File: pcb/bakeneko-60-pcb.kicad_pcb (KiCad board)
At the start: 2 copper layers, 284.7 x 94.2 mm, 147 parts, among them J1 JST SH 4-pin, J2 AVR-ISP-6, SW1 Reset, U1 SRV05-4, U2 ATmega32U4-AU, Y1 16MHz

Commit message: add fn1
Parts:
- added D64: 1N4148, Diode_SMD:D_SOD-123, F.Cu at (68.7, 86.1)
- added MX74: 1.25u, MX_Only:MXOnly-1.25U-NoLED, F.Cu at (82.8, 85.2)
- MX69: value 1.5u -> 1.25u; footprint MX_Only:MXOnly-1.5U-NoLED -> MX_Only:MXOnly-1.25U-NoLED
- MX70: value 7u -> 2.75u; footprint MX_Only:MXOnly-7U-ReversedStabilizers-NoLED -> MX_Only:MXOnly-2.75U-ReversedStabilizers-NoLED
- moved MX69 2.38 mm to (59.0, 85.2)
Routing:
- net COL4: track 143.4 -> 165.4 mm
- net Net-(D64-Pad2): track 0.00 -> 11.1 mm
- net Net-(D58-Pad2): track 9.20 -> 6.82 mm
- net COL2: track 142.7 -> 143.7 mm

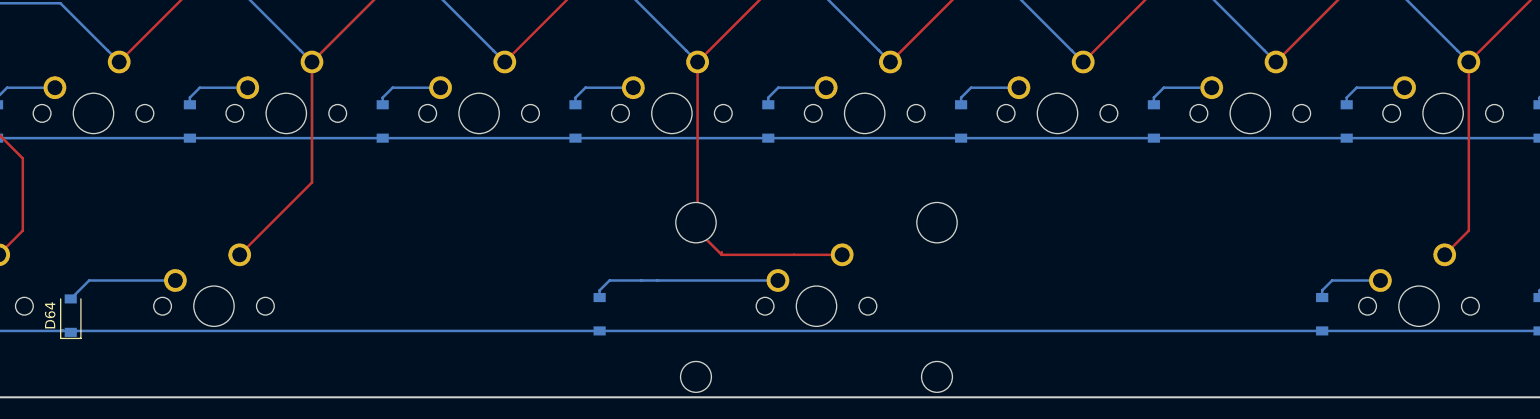
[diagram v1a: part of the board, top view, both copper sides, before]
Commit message: bottom row done except for diodes wrong side
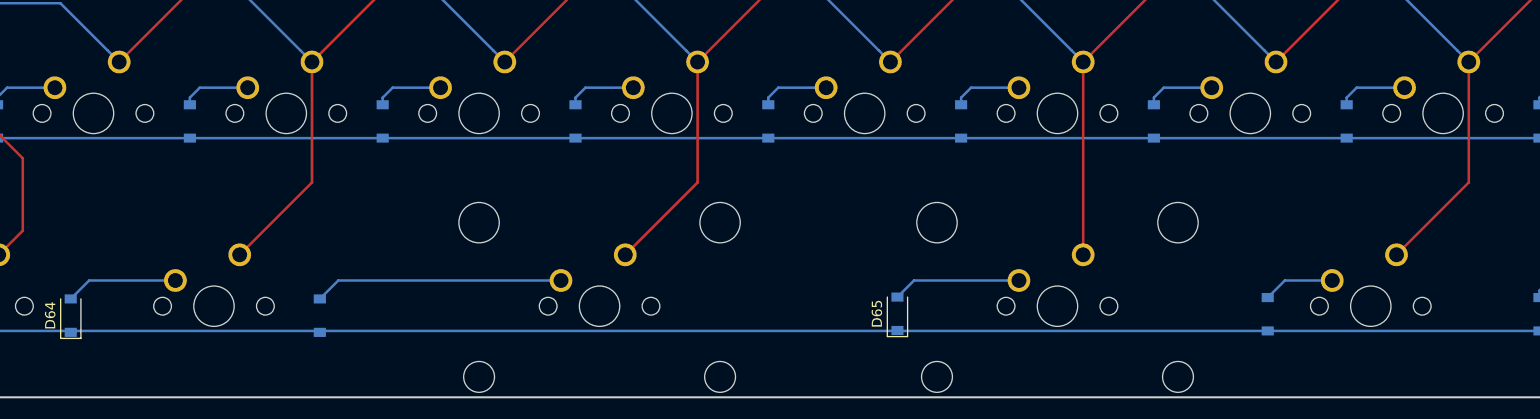
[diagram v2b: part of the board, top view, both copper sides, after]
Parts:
- added D65: 1N4148, Diode_SMD:D_SOD-123, F.Cu at (150.3, 86.0)
- added MX75: 2u, MX_Only:MXOnly-2U-ReversedStabilizers-NoLED, F.Cu at (166.2, 85.2)
- moved D59 27.6 mm to (93.3, 86.1)
- moved MX70 21.4 mm to (120.9, 85.2)
- moved D60 5.38 mm to (186.9, 86.0)
- moved MX63 4.76 mm to (197.1, 85.2)
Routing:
- net COL8: track 217.4 -> 236.4 mm
- net Net-(MX75-Pad1): track 0.00 -> 12.7 mm
- net COL6: track 212.3 -> 202.1 mm
- net Net-(D59-Pad2): track 18.7 -> 24.6 mm
- net COL10: track 274.7 -> 276.7 mm

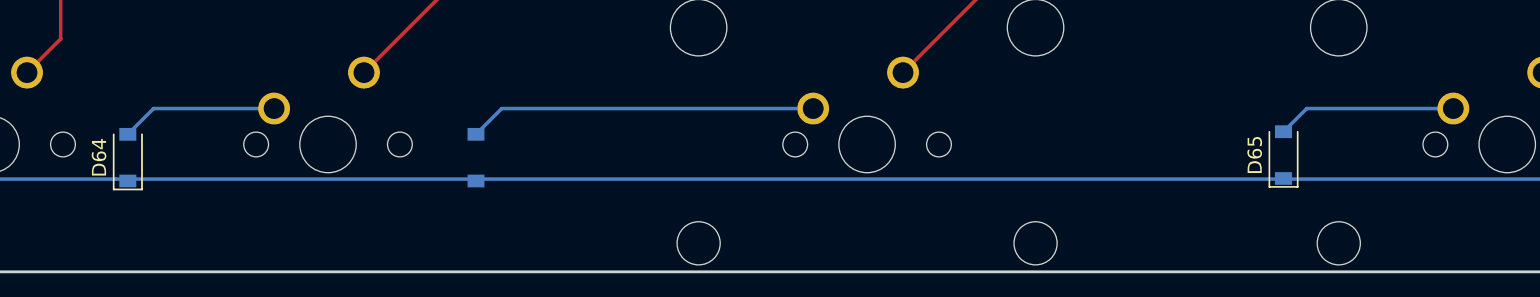
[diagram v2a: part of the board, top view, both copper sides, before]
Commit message: bottom row done
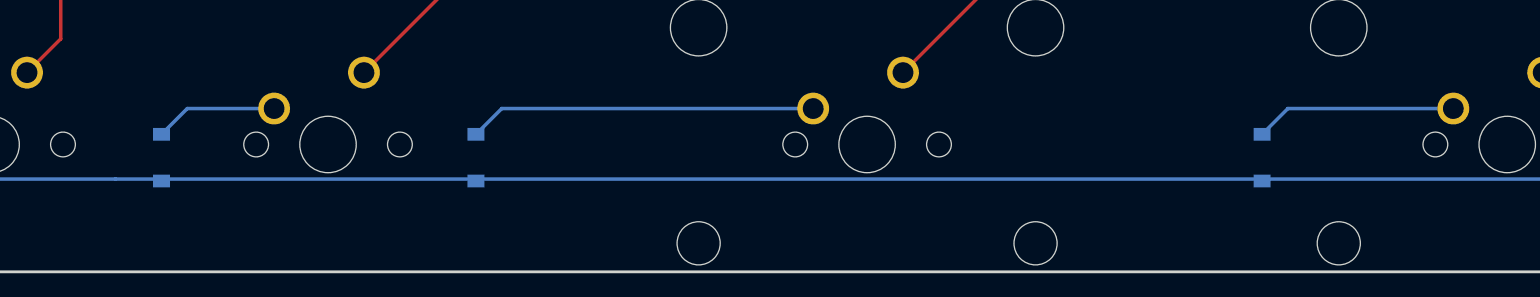
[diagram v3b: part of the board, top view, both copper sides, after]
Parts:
- D64, D65: moved to B.Cu
- moved D64 2.38 mm to (71.0, 86.1)
- moved D65 1.52 mm to (148.8, 86.1)
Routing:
- net Net-(D64-Pad2): track 11.1 -> 8.71 mm
- net Net-(MX75-Pad1): track 12.7 -> 14.3 mm
